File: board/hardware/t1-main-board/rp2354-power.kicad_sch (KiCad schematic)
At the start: 27 parts, among them U3501 RP2354A, U3502 TPS22919DCKR, U3503 TPS22919DCKR

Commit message: Zone net classes and named switch nodes from the generator
Every net but GND now carries the ZONE_<NAME> class of each zone whose
blocks it touches (block zones from pcb/plan.py; the faceplate connector's
sheet also the faceplate zone); a rail used in more than one zone carries
ZONE_SHARED. Nets KiCad names from a pin take their part's sheet zone.
1,080 nets: 911 in one zone, 104 in two, 36 in three, 28 shared rails.

Switch nodes are named *_SW (VSYS_LV_SW, VCC3V3_SYS_SW, VDD_CPU_SW,
RP_VREG_SW); the display switch output is FP_VCI_OUT, so SW_NODE holds
the 18 switch nodes only. Board rebuilt: DRC 0 errors, 607 warnings
(the six PCB-I-09 gone), ERC 0 errors, craft Q1 met, pcb tests pass.
Closes placement v1 open items 2 and 3, floorplan v1 item 6.

Co-Authored-By: Claude Opus 5.5 <noreply@anthropic.com>
Claude-Session: https://claude.ai/code/session_01Ei262h3TpgY9vyfNLMi5Mn
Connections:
- net RP_VREG_LX renamed RP_VREG_SW
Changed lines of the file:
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@@
 (label "RP_DVDD" (at 82.55 59.69 90) (effects (font (size 1.27 1.27)) (justify left bottom)))
 (label "RP_DVDD" (at 36.83 87.63 180) (effects (font (size 1.27 1.27)) (justify right bottom)))
-(label "RP_VREG_LX" (at 97.79 87.63 0) (effects (font (size 1.27 1.27)) (justify left bottom)))
+(label "RP_VREG_SW" (at 97.79 87.63 0) (effects (font (size 1.27 1.27)) (justify left bottom)))
 (label "RP_VREG_AVDD" (at 77.47 62.23 90) (effects (font (size 1.27 1.27)) (justify left bottom)))
 (label "RP_DVDD" (at 115.57 106.68 90) (effects (font (size 1.27 1.27)) (justify left bottom)))
@@
 (label "RP_VREG_AVDD" (at 175.26 106.68 90) (effects (font (size 1.27 1.27)) (justify left bottom)))
 (label "RP_DVDD" (at 115.57 160.02 270) (effects (font (size 1.27 1.27)) (justify right bottom)))
-(label "RP_VREG_LX" (at 115.57 149.86 90) (effects (font (size 1.27 1.27)) (justify left bottom)))
+(label "RP_VREG_SW" (at 115.57 149.86 90) (effects (font (size 1.27 1.27)) (justify left bottom)))
 (label "RP_PWR_EN" (at 223.52 55.88 180) (effects (font (size 1.27 1.27)) (justify right bottom)))
 (label "RP_3V3_SRC" (at 248.92 53.34 0) (effects (font (size 1.27 1.27)) (justify left bottom)))

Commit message: Compaction: lower inductors, 0201 decoupling, 0.8 mm signal test pads
A matrix tool (hardware/studies/compaction) checks each candidate against
the design's stresses: same inductance, design peak <= 70 % and the
converter's maximum limit <= 100 % of Isat (30 % drop), height zones,
ratings at least twice the rail, PCB-D-06; sourcing outcome per part.

Applied (placement v1 decision 12, BOM v1.15):
- L601, L4401: XGL4015-102MEC (1.5 mm) for XAL/XGL4020-102MEC (2.1 mm);
- L1001, L5101: XGL4015-471MEC (1.5 mm) for Wurth 744373240047, on the
  stock XxL4020 land (the Wurth land was never drawn);
- L1201 is 1.2 mm (XGL4012, per-MPN heights): it moves next to the SoC;
- 58 x 100 nF decoupling on rails <= 3.3 V in core/IO/radio: 0201;
- 51 test pads on signal nets: 0.8 mm (PCB-D-06 v0.16, JLCPCB guide).
Kept: L901, L2802 (XGL4015 at 103 % of Isat at the limit); no thinner
0805/1206 capacitor passes (obsolete, NRND or unlisted).

Board need 113 % -> 111 % (core band 227 -> 203 %, power band 258 ->
233 %, radio band 19 -> 0 %); only C904 still relies on PCB-Z-04.
ERC 0 errors, craft Q1 met, DRC 0 errors (605 warnings), pcb and study
tests pass, rules test board PASS.

Co-Authored-By: Claude Opus 5.5 <noreply@anthropic.com>
Claude-Session: https://claude.ai/code/session_01Ei262h3TpgY9vyfNLMi5Mn
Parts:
- C3502, C3503, C3504, C3505, C3506, C3507, C3509, C3510, C3511, C3513, C3514: footprint Capacitor_SMD:C_0402_1005Metric -> Capacitor_SMD:C_0201_0603Metric; MPN GRM155R71C104KA88D -> GRM033R61A104KE15D

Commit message: Board on libs v0.2.0: lower-case kebab vendor keys (HL-13)
The libs submodule moves to v0.2.0 (5f24483). Every library nickname in
the generator, the placement tool and the floorplan study follows the
key table (Texas_Instruments -> texas-instruments, OpenDAP_Device ->
opendap-generic, Rockchip and Rockchip_PMIC -> rockchip, ...); the
library tables are written from the files. Schematic and board
regenerated.

Checks: ERC 0 errors (warnings unchanged); DRC 0 errors, 605 warnings,
the same counts by type, schematic parity 0; every placement identical;
craft Q1 met; pcb tests pass; STEP export resolves every libs 3D model
(the 27 parts without a model are KiCad stock lands that have none).

Co-Authored-By: Claude Opus 5.5 <noreply@anthropic.com>
Claude-Session: https://claude.ai/code/session_01Ei262h3TpgY9vyfNLMi5Mn
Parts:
- U3501: footprint Raspberry_Pi:QFN-60-1EP_7x7mm_P0.4mm_EP3.4x3.4mm_ThermalVias -> raspberry-pi:QFN-60-1EP_7x7mm_P0.4mm_EP3.4x3.4mm_ThermalVias; symbol Raspberry_Pi:RP2354A -> raspberry-pi:RP2354A
- U3502, U3503: footprint Texas_Instruments:Texas_DCK0006A_SC-70-6_1.25x2mm_P0.65mm -> texas-instruments:Texas_DCK0006A_SC-70-6_1.25x2mm_P0.65mm; symbol Texas_Instruments:TPS22919DCKR -> texas-instruments:TPS22919DCKR
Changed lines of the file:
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@@
 (paper "A3")
 (title_block (title "Coprocessor: supplies") (date "2026-10-25") (rev "A") (company "The OpenDAP Project") (comment 1 "blk.rp2354-power") (comment 2 "RP2354A supply unit, core regulator, RP_3V3 and RP_IOVDD_1V8 switches and links"))
-(symbol (lib_id "Raspberry_Pi:RP2354A") (at 67.31 87.63 0) (unit 3) (body_style 1) (exclude_from_sim no) (in_bom yes) (on_board yes) (dnp no)
+(symbol (lib_id "raspberry-pi:RP2354A") (at 67.31 87.63 0) (unit 3) (body_style 1) (exclude_from_sim no) (in_bom yes) (on_board yes) (dnp no)
   (property "Reference" "U3501" (at 88.9 66.04 0) (effects (font (size 1.27 1.27)) (justify left)))
   (property "Value" "RP2354A" (at 88.9 63.5 0) (effects (font (size 1.27 1.27)) (justify left)))
-  (property "Footprint" "Raspberry_Pi:QFN-60-1EP_7x7mm_P0.4mm_EP3.4x3.4mm_ThermalVias" (at 67.31 87.63 0) (effects (font (size 1.27 1.27))) (hide yes))
+  (property "Footprint" "raspberry-pi:QFN-60-1EP_7x7mm_P0.4mm_EP3.4x3.4mm_ThermalVias" (at 67.31 87.63 0) (effects (font (size 1.27 1.27))) (hide yes))
   (property "Datasheet" "https://datasheets.raspberrypi.com/rp2350/rp2350-datasheet.pdf" (at 67.31 87.63 0) (effects (font (size 1.27 1.27))) (hide yes))
   (property "Description" "RP2350 microcontroller with 2 MB of QSPI flash stacked in the package, 30 GPIOs, QFN-60 7 x 7 mm, 0.4 mm pitch, exposed GND pad" (at 67.31 87.63 0) (effects (font (size 1.27 1.27))) (hide yes))
@@
 (rectangle (start 22.86 35.56) (end 201.93 176.53) (stroke (width 0) (type dash)) (fill (type none)))
 (text "RP2354A supplies, core regulator (DS §6.1, §6.3.8; HDG §2.2.1)" (exclude_from_sim no) (at 24.13 34.29 0) (effects (font (size 2.54 2.54)) (justify left bottom)))
-(symbol (lib_id "Texas_Instruments:TPS22919DCKR") (at 236.22 58.42 0) (unit 1) (body_style 1) (exclude_from_sim no) (in_bom yes) (on_board yes) (dnp no)
+(symbol (lib_id "texas-instruments:TPS22919DCKR") (at 236.22 58.42 0) (unit 1) (body_style 1) (exclude_from_sim no) (in_bom yes) (on_board yes) (dnp no)
   (property "Reference" "U3502" (at 228.6 43.18 0) (effects (font (size 1.27 1.27)) (justify left)))
   (property "Value" "TPS22919DCKR" (at 228.6 40.64 0) (effects (font (size 1.27 1.27)) (justify left)))
-  (property "Footprint" "Texas_Instruments:Texas_DCK0006A_SC-70-6_1.25x2mm_P0.65mm" (at 236.22 58.42 0) (effects (font (size 1.27 1.27))) (hide yes))
+  (property "Footprint" "texas-instruments:Texas_DCK0006A_SC-70-6_1.25x2mm_P0.65mm" (at 236.22 58.42 0) (effects (font (size 1.27 1.27))) (hide yes))
   (property "Datasheet" "https://www.ti.com/lit/ds/symlink/tps22919.pdf" (at 236.22 58.42 0) (effects (font (size 1.27 1.27))) (hide yes))
   (property "Description" "Load switch, 1.6-5.5 V, 1.5 A, 90 mOhm, controlled rise time, short-circuit protection, adjustable quick output discharge, SOT/SC-70-6 (DCK0006A)" (at 236.22 58.42 0) (effects (font (size 1.27 1.27))) (hide yes))
@@
 (rectangle (start 207.01 35.56) (end 279.4 85.09) (stroke (width 0) (type dash)) (fill (type none)))
 (text "RP_3V3 switch (BOM v1 line 50)" (exclude_from_sim no) (at 208.28 34.29 0) (effects (font (size 2.54 2.54)) (justify left bottom)))
-(symbol (lib_id "Texas_Instruments:TPS22919DCKR") (at 233.68 118.11 0) (unit 1) (body_style 1) (exclude_from_sim no) (in_bom yes) (on_board yes) (dnp no)
+(symbol (lib_id "texas-instruments:TPS22919DCKR") (at 233.68 118.11 0) (unit 1) (body_style 1) (exclude_from_sim no) (in_bom yes) (on_board yes) (dnp no)
   (property "Reference" "U3503" (at 226.06 102.87 0) (effects (font (size 1.27 1.27)) (justify left)))
   (property "Value" "TPS22919DCKR" (at 226.06 100.33 0) (effects (font (size 1.27 1.27)) (justify left)))
-  (property "Footprint" "Texas_Instruments:Texas_DCK0006A_SC-70-6_1.25x2mm_P0.65mm" (at 233.68 118.11 0) (effects (font (size 1.27 1.27))) (hide yes))
+  (property "Footprint" "texas-instruments:Texas_DCK0006A_SC-70-6_1.25x2mm_P0.65mm" (at 233.68 118.11 0) (effects (font (size 1.27 1.27))) (hide yes))
   (property "Datasheet" "https://www.ti.com/lit/ds/symlink/tps22919.pdf" (at 233.68 118.11 0) (effects (font (size 1.27 1.27))) (hide yes))
   (property "Description" "Load switch, 1.6-5.5 V, 1.5 A, 90 mOhm, controlled rise time, short-circuit protection, adjustable quick output discharge, SOT/SC-70-6 (DCK0006A)" (at 233.68 118.11 0) (effects (font (size 1.27 1.27))) (hide yes))

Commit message: Board in the 62.5 x 95.0 mm body: ADR 0025, outline 59.1 x 91.6, 0201 swaps
ADR 0025 supersedes ADR 0016 for t1 ADR 0006's body: board outline from
the body, 1.2 mm walls and 0.5 mm clearance; height zones and stack
restated unchanged; the speaker on a case shelf (PCB-Z-09); pocket
reliefs at the 4.4 mm jack, the microSD (DM3AT push-push kept) and the
side buttons; the audio 0603 -> 0402 swap gated by t1 V2-A08; reserve
(NFC reader, then TPM) recorded, not applied.

- pcb/geometry.py derives the outline from BODY, WALL and CLEARANCE;
  the pocket, display and fixed parts keep their device-frame positions;
  holes keep their edge distance; the speaker shadow becomes a 1.5 mm
  shelf height area (placement, checks, occupancy).
- build.py reports pocket reliefs and routing room; C904 unfixed (it
  now finds back room, so PCB-Z-04 carries no part).
- Generator: parts.area_swap puts 121 generic 0402 resistors (outside
  audio and VBUS paths, >= 10 ohm) and five 100 nF signal capacitors in
  0201 (BOM v1.16); schematic and board regenerated.
- Result: 1,012/1,012 placed, 98.8 % by the floorplan method (was 111 %),
  factor left 1.68 (was 1.49); DRC 0 errors, ERC 0 errors, 0 check
  findings, pcb tests 20/20, schematic craft Q1 met.
- Specs: PCB constraints v0.17 (M-01, M-02, M-08, Z-02, Z-06 to Z-09,
  R-07), placement v1.1 (section 3, decisions 4 and 13, checks, open
  items with the gated swaps and the reserve), floorplan v1 section 1,
  BOM v1.16.

Co-Authored-By: Claude Opus 5.5 <noreply@anthropic.com>
Claude-Session: https://claude.ai/code/session_01Ei262h3TpgY9vyfNLMi5Mn
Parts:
- R3512: footprint Resistor_SMD:R_0402_1005Metric -> Resistor_SMD:R_0201_0603Metric; MPN RC0402FR-0733RL -> RC0201FR-0733RL
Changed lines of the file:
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@@
   (property "Reference" "R3512" (at 163.83 111.76 0) (effects (font (size 1.27 1.27)) (justify left)))
   (property "Value" "33 Ω" (at 163.83 114.3 0) (effects (font (size 1.27 1.27)) (justify left)))
-  (property "Footprint" "Resistor_SMD:R_0402_1005Metric" (at 162.56 113.03 0) (effects (font (size 1.27 1.27))) (hide yes))
-  (property "Datasheet" "https://yageogroup.com/en/ProductSearch/PartNumberSearch?part=RC0402FR-0733RL" (at 162.56 113.03 0) (effects (font (size 1.27 1.27))) (hide yes))
-  (property "Description" "Resistor, 33 Ω, 1 %, 1/16 W, 0402" (at 162.56 113.03 0) (effects (font (size 1.27 1.27))) (hide yes))
+  (property "Footprint" "Resistor_SMD:R_0201_0603Metric" (at 162.56 113.03 0) (effects (font (size 1.27 1.27))) (hide yes))
+  (property "Datasheet" "https://yageogroup.com/en/ProductSearch/PartNumberSearch?part=RC0201FR-0733RL" (at 162.56 113.03 0) (effects (font (size 1.27 1.27))) (hide yes))
+  (property "Description" "Resistor, 33 Ω, 1 %, 1/20 W, 0201" (at 162.56 113.03 0) (effects (font (size 1.27 1.27))) (hide yes))
   (property "Manufacturer" "YAGEO" (at 162.56 113.03 0) (effects (font (size 1.27 1.27))) (hide yes))
-  (property "MPN" "RC0402FR-0733RL" (at 162.56 113.03 0) (effects (font (size 1.27 1.27))) (hide yes))
+  (property "MPN" "RC0201FR-0733RL" (at 162.56 113.03 0) (effects (font (size 1.27 1.27))) (hide yes))
   (property "Block" "blk.rp2354-power" (at 162.56 113.03 0) (effects (font (size 1.27 1.27))) (hide yes))
   (pin "1")

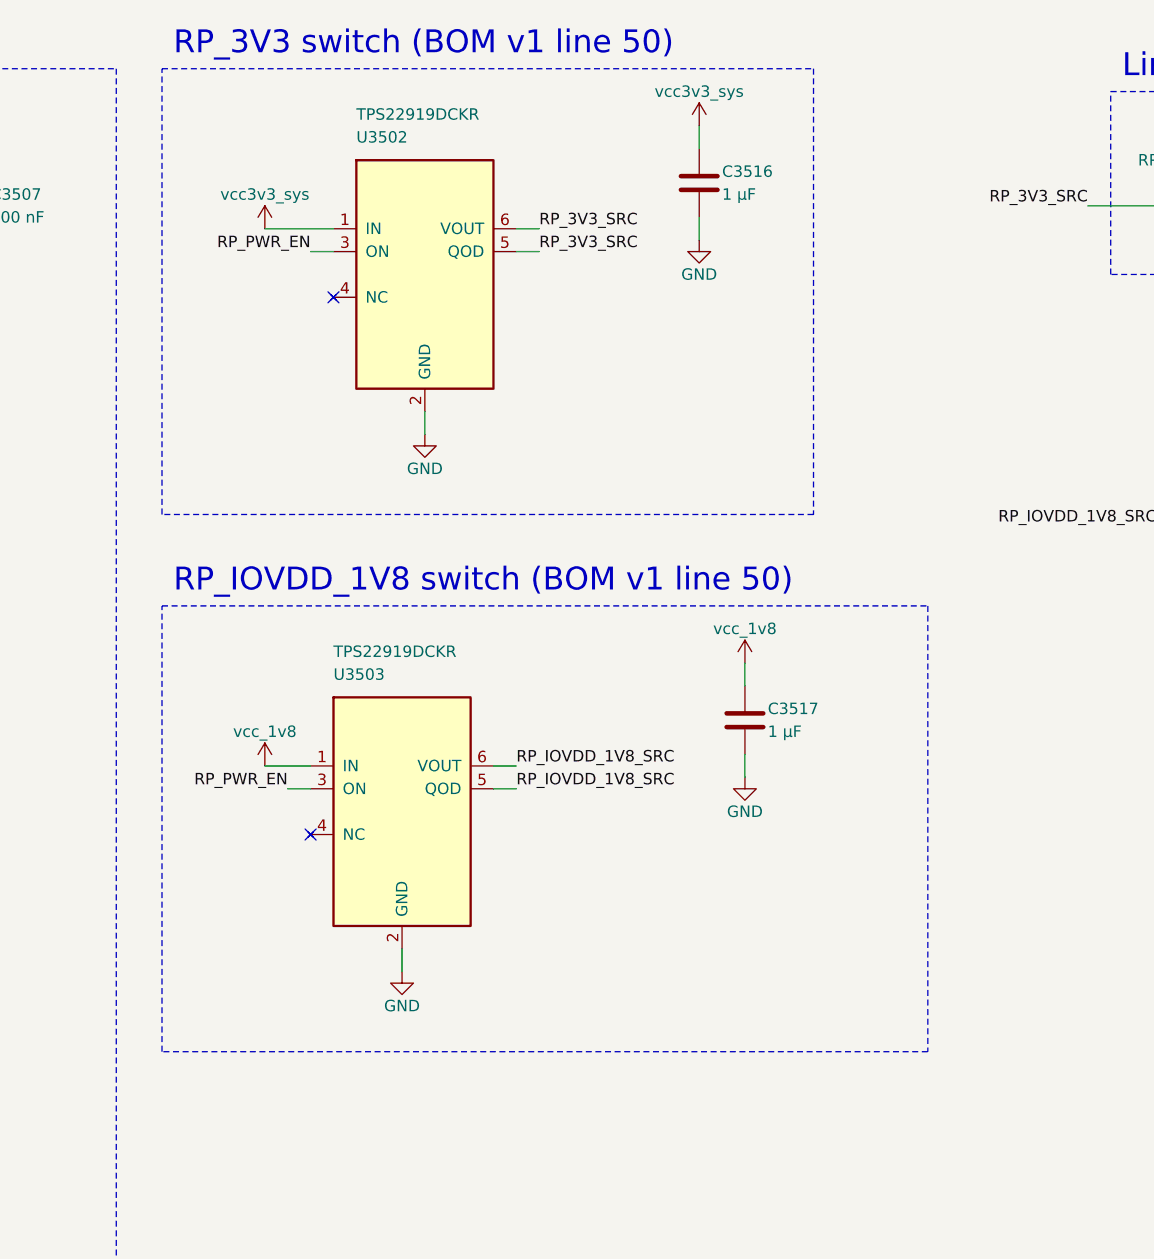
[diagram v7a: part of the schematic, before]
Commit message: Load switches in TPS22916C WCSP (BOM v1.17 item 3, libs v0.3.1)
The six TPS22919DCKR become the TPS22916CYFPR, the BOM's named second
source, now that kicad-lib v0.3.1 carries its land, symbol and model.
Each position's rise time and output discharge checked against the
data sheet (SLVSDO5F section 6.6): every sequencing rule holds; the
fixed 150 Ohm discharge is slower and the driver's delays follow it.
Power tree v0.9 restates the switch rows.

Co-Authored-By: Claude Opus 5.5 <noreply@anthropic.com>
Claude-Session: https://claude.ai/code/session_01Ei262h3TpgY9vyfNLMi5Mn
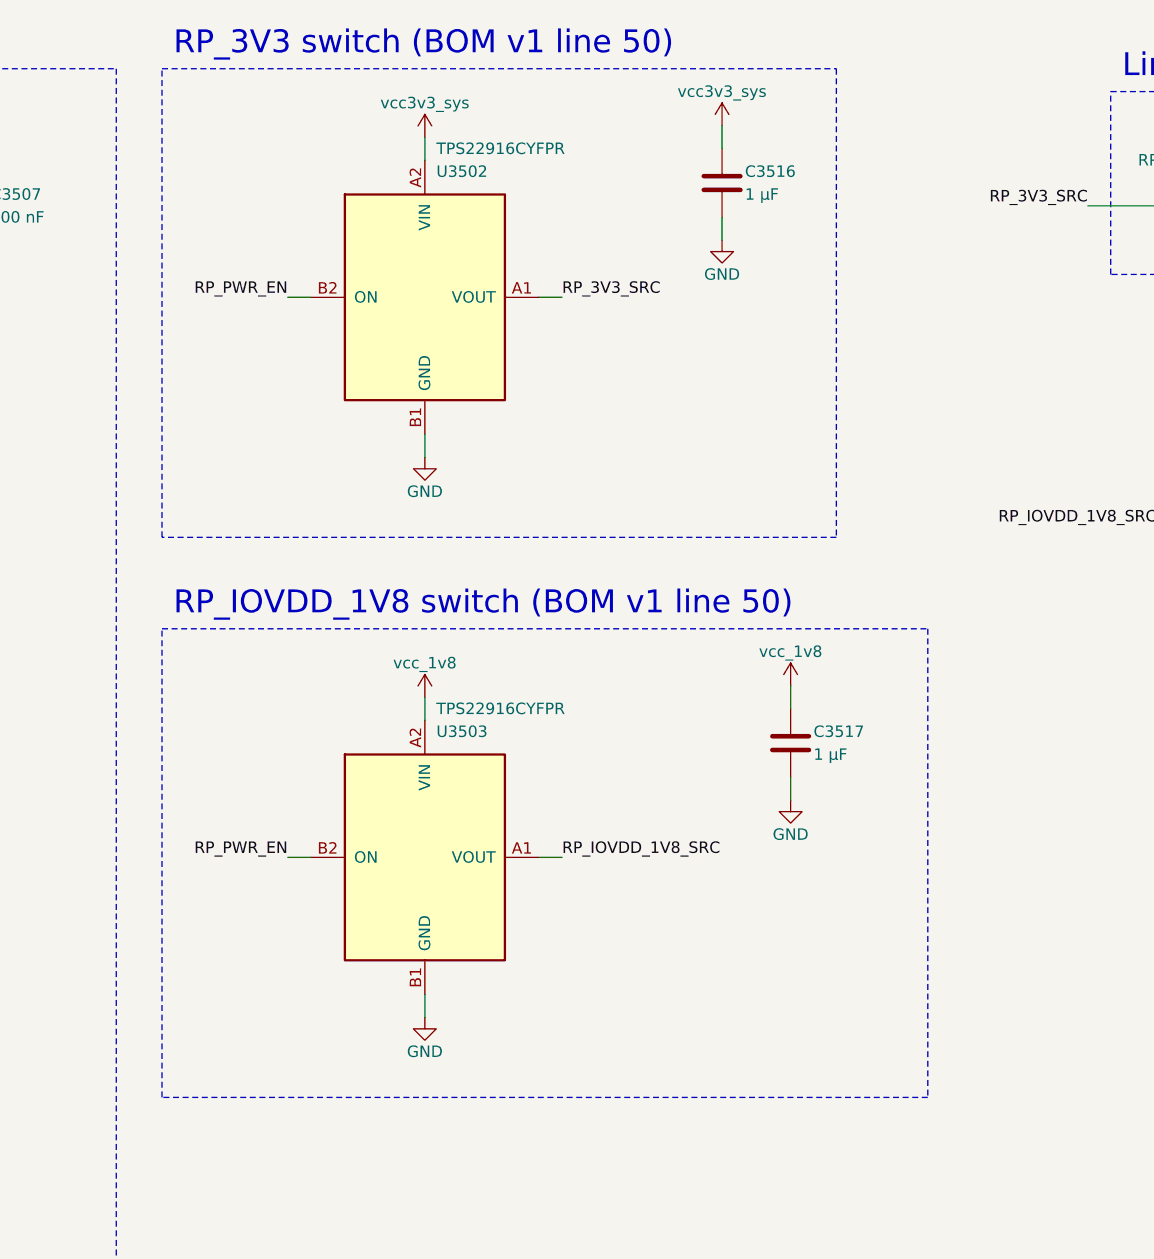
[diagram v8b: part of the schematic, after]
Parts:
- U3502, U3503: value TPS22919DCKR -> TPS22916CYFPR; footprint texas-instruments:Texas_DCK0006A_SC-70-6_1.25x2mm_P0.65mm -> texas-instruments:Texas_YFP0004_DSBGA-4_0.78x0.78mm_Layout2x2_P0.4mm; symbol texas-instruments:TPS22919DCKR -> texas-instruments:TPS22916CYFPR; MPN TPS22919DCKR -> TPS22916CYFPR; Second_Source Texas Instruments TPS22916CYFPR (WCSP, other land; BOM v1 l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 -> (none)
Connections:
- net GND: now also U3502.B1 (GND), U3503.B1 (GND); no longer U3502.2 (GND), U3503.2 (GND)
- net RP_3V3_SRC: now also U3502.A1 (VOUT); no longer U3502.5 (QOD), U3502.6 (VOUT)
- net RP_IOVDD_1V8_SRC: now also U3503.A1 (VOUT); no longer U3503.5 (QOD), U3503.6 (VOUT)
- net RP_PWR_EN: now also U3502.B2 (ON), U3503.B2 (ON); no longer U3502.3 (ON), U3503.3 (ON)
- net vcc3v3_sys: now also U3502.A2 (VIN); no longer U3502.1 (IN)
- net vcc_1v8: now also U3503.A2 (VIN); no longer U3503.1 (IN)
- no-connect marks 2 -> 0
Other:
- moved on the sheet: C3516, C3517
